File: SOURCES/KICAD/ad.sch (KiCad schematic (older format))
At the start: 154 parts, among them IC201 IC_OPA1652AIDR, IC202 IC_OPA1652AIDR, IC203 IC_OPA1652AIDR, IC204 IC_OPA1652AIDR, IC205 IC_AK5558VN, IC206 IC_OPA1652AIDR, IC207 IC_OPA1652AIDR, IC208 IC_OPA1652AIDR, IC209 IC_OPA1652AIDR, X201 CONN_02X13

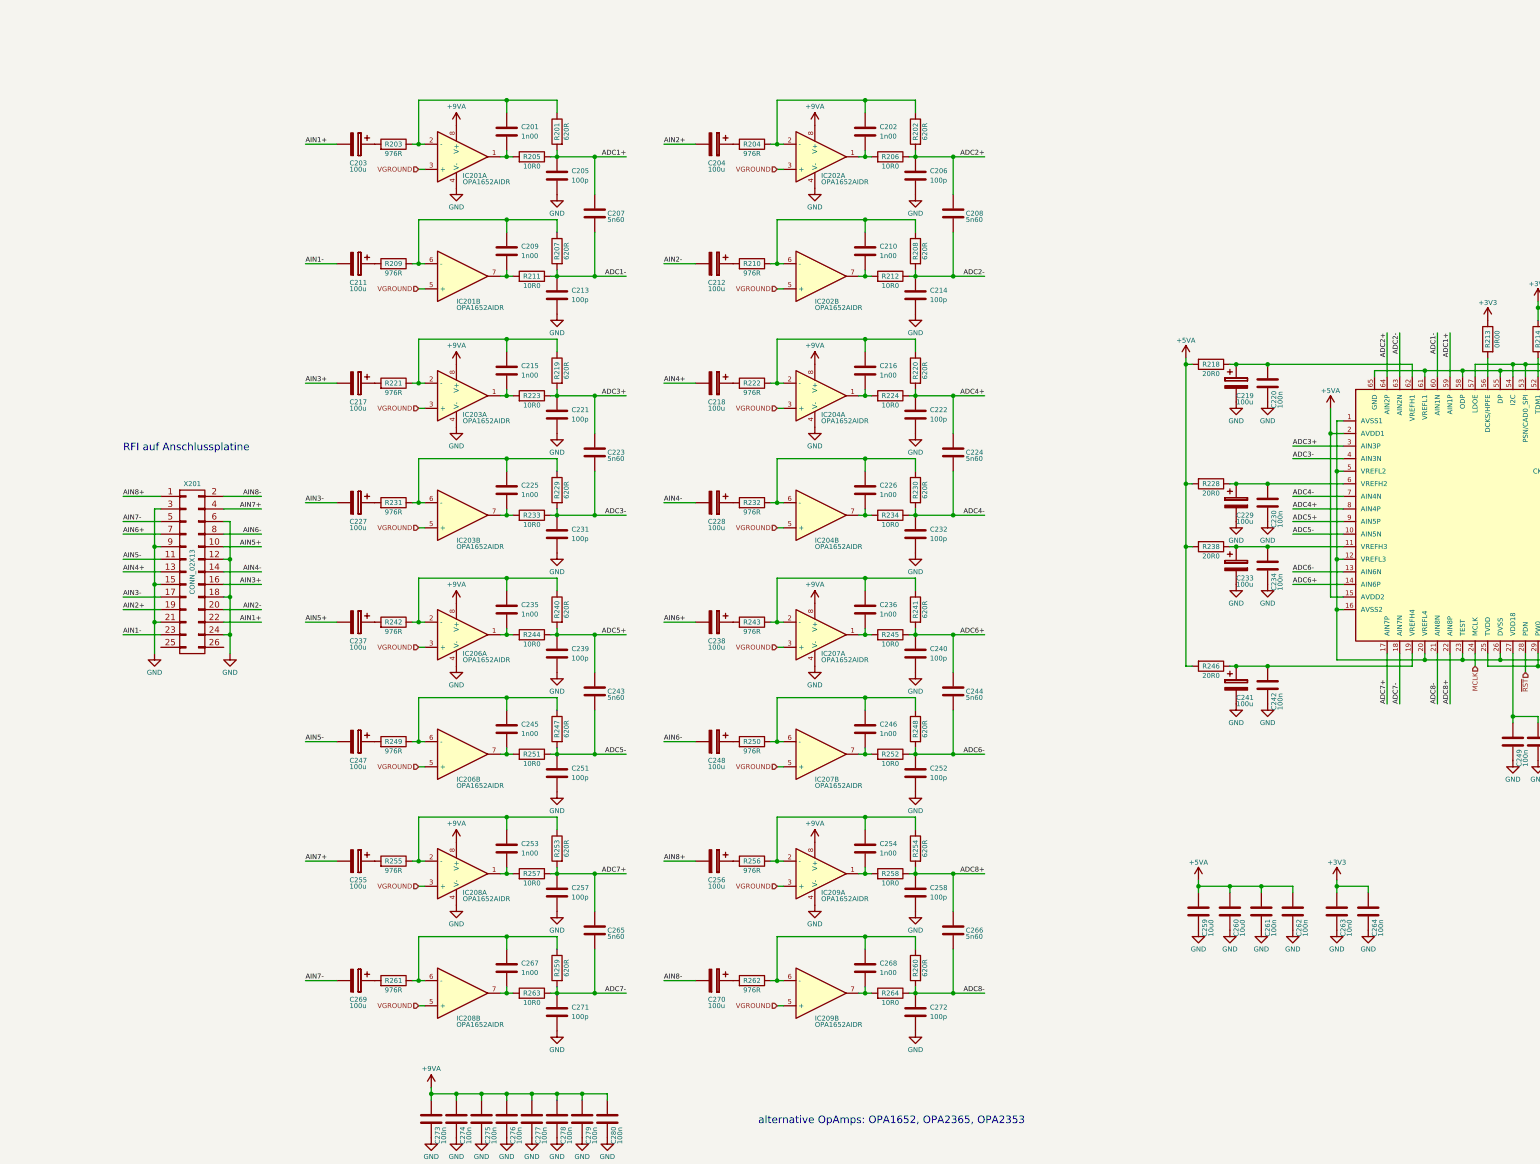
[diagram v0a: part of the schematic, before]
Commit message: Improved ADC input stage
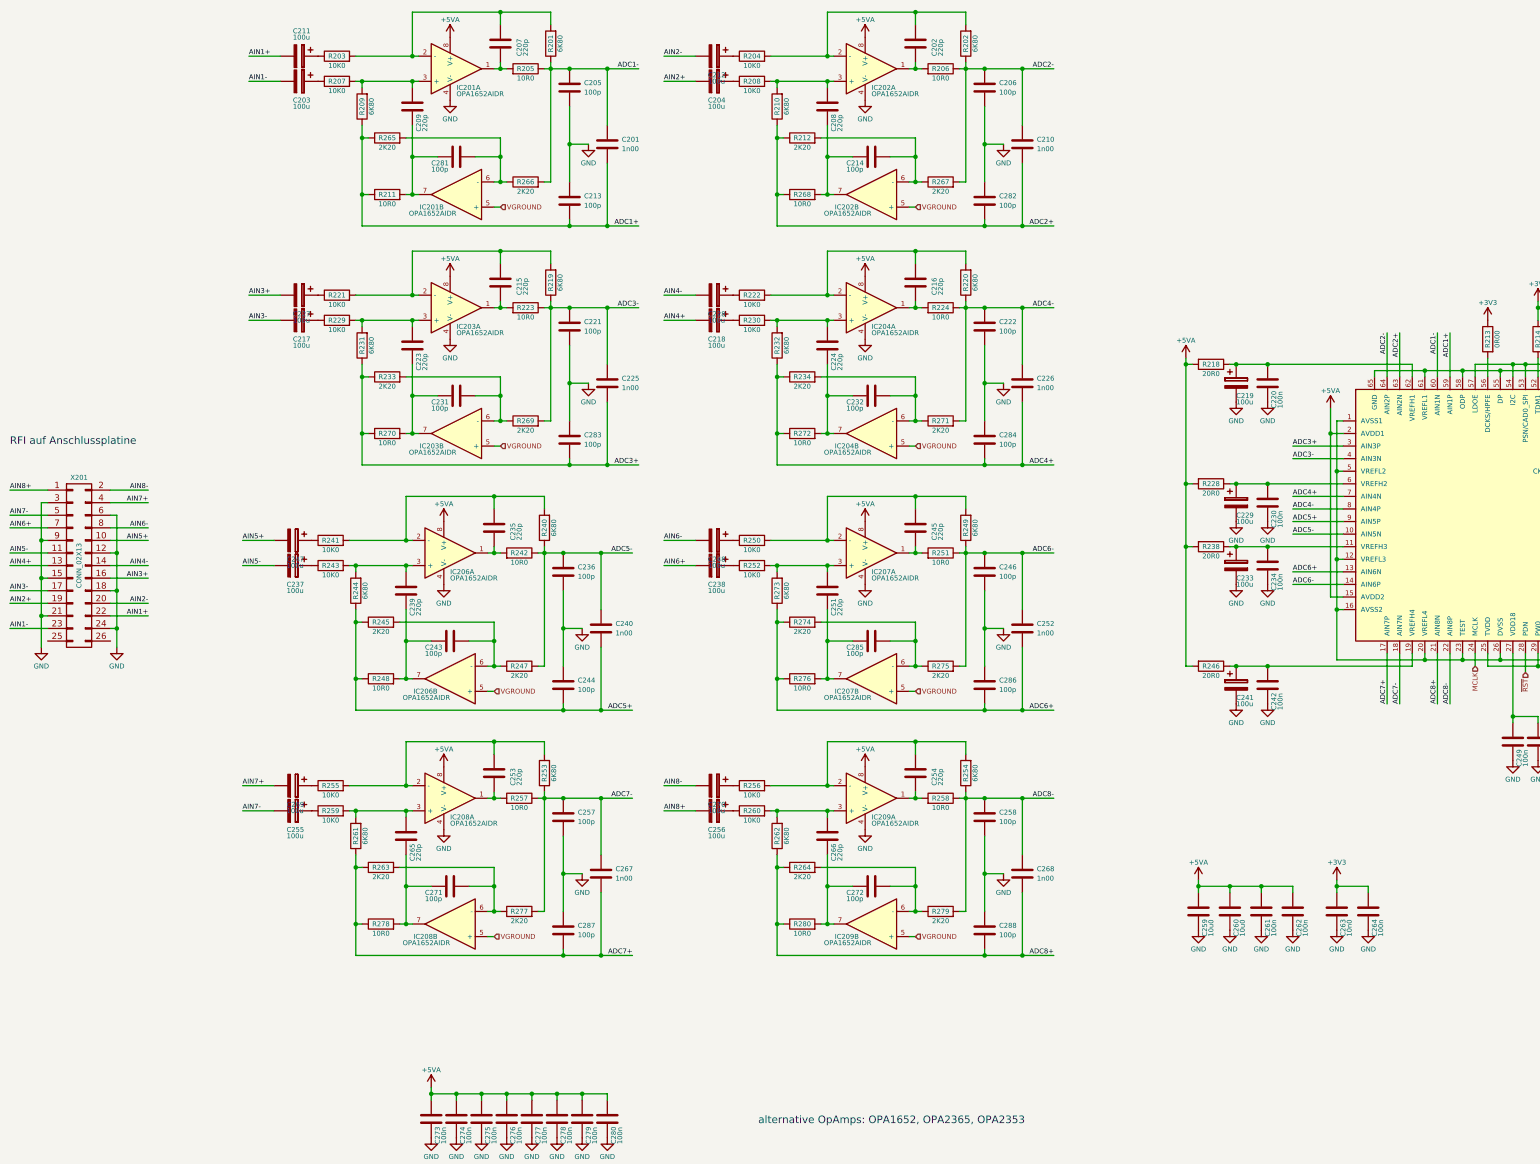
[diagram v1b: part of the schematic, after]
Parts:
- removed C207, C208, C223, C224, C243, C244, C265, C266: CAP_5n60_5%_16V_PPS_0805, rklib:C0805-X7R, symbol rk:CAP_5n60_5%_16V_PPS_0805
- removed C236, C246: CAP_1n00_5%_50V_PPS_0805, rklib:C0805-X7R, symbol rk:CAP_1n00_5%_50V_PPS_0805
- removed C239, C240, C251, C252: CAP_100p_50V_C0G_NP0_0805, rklib:C0805-X7R, symbol rk:CAP_100p_50V_C0G_NP0_0805
- removed R201, R202, R207, R208, R219, R220, R229, R230, R240, R241, R247, R248, R253, R254, R259, R260: RES_620R_0.5%_0.1W_Thin_0805, rklib:C0805-RES, symbol rk:RES_620R_0.5%_0.1W_Thin_0805
- removed R203, R204, R209, R210, R221, R222, R231, R232, R242, R243, R249, R250, R255, R256, R261, R262: RES_976R_0.5%_0.1W_Thin_0805, rklib:C0805-RES, symbol rk:RES_976R_0.5%_0.1W_Thin_0805
- removed R212, R233, R234, R244, R245, R252, R263, R264: RES_10R0_1%_0.25W_Thin_0805, rklib:C0805-RES, symbol rk:RES_10R0_1%_0.25W_Thin_0805
- added C207, C208, C223, C224, C239, C251, C265, C266: CAP_220p_2%_50V_PPS_0805, rklib:C0805-X7R, symbol rk:CAP_1n00_5%_50V_PPS_0805
- added C236, C243, C244, C246, C281, C282, C283, C284, C285, C286, C287, C288: CAP_100p_50V_C0G_NP0_0805, rklib:C0805-X7R, symbol rk:CAP_100p_50V_C0G_NP0_0805
- added C240, C252: CAP_1n00_5%_50V_PPS_0805, rklib:C0805-X7R, symbol rk:CAP_1n00_5%_50V_PPS_0805
- added R201, R202, R209, R210, R219, R220, R231, R232, R240, R244, R249, R253, R254, R261, R262, R273: RES_6K80_1%_0.25W_Thin_0805, rklib:C0805-RES, symbol rk:RES_10K0_1%_0.25W_Thin_0805
- added R203, R204, R207, R208, R221, R222, R229, R230, R241, R243, R250, R252, R255, R256, R259, R260: RES_10K0_1%_0.25W_Thin_0805, rklib:C0805-RES, symbol rk:RES_10K0_1%_0.25W_Thin_0805
- added R212, R233, R234, R245, R247, R263, R264, R265, R266, R267, R269, R271, R274, R275, R277, R279: RES_2K20_1%_0.25W_Thin_0805, rklib:C0805-RES, symbol rk:RES_10K0_1%_0.25W_Thin_0805
- added R242, R248, R268, R270, R272, R276, R278, R280: RES_10R0_1%_0.25W_Thin_0805, rklib:C0805-RES, symbol rk:RES_10R0_1%_0.25W_Thin_0805
- C202, C209, C215, C216, C235, C245, C253, C254: value CAP_1n00_5%_50V_PPS_0805 -> CAP_220p_2%_50V_PPS_0805; Value1 1n00 -> 220p; Value2 5% 50V PPS -> 2% 50V PPS; digikey PCF1328CT-ND -> PCF1288CT-ND; pn ECH-U1H102JX5 -> ECH-U1H221GX5
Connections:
- net +9VA is gone; now on net +5VA: C273.1, C274.1, C275.1, C276.1, C277.1, C278.1, C279.1, C280.1, IC201.8 (V+), IC202.8 (V+), IC203.8 (V+), IC204.8 (V+), IC206.8 (V+), IC207.8 (V+), IC208.8 (V+), IC209.8 (V+)
- net ADC1+: now also C201.2, C213.2, R211.1, R209.1, R265.1; no longer C205.1, R205.1
- net ADC1-: now also C201.1, C205.1, R205.1, R201.1, R266.2; no longer C213.1, R211.1
- net ADC2+: now also C210.2, IC205.63 (AIN2N), C282.2, R210.1, R212.1, R268.1; no longer C206.1, IC205.64 (AIN2P), R206.1
- net ADC2-: now also C206.1, C210.1, IC205.64 (AIN2P), R206.1, R202.1, R267.2; no longer C214.1, IC205.63 (AIN2N)
- net ADC3+: now also C225.2, C283.2, R231.1, R233.1, R270.1; no longer C221.1, R223.1
- net ADC3-: now also C221.1, C225.1, R223.1, R219.1, R269.2; no longer C231.1
- net ADC4+: now also C226.2, IC205.7 (AIN4N), C284.2, R232.1, R234.1, R272.1; no longer C222.1, IC205.8 (AIN4P), R224.1
- net ADC4-: now also C222.1, C226.1, IC205.8 (AIN4P), R224.1, R220.1, R271.2; no longer C232.1, IC205.7 (AIN4N)
- net ADC5+: now also C240.2, C244.2, R244.1, R245.1, R248.1
- net ADC5-: now also C236.1, C240.1, R240.1, R242.1, R247.2; no longer R251.1
- net ADC6+: now also IC205.13 (AIN6N), C252.2, C286.2, R273.1, R274.1, R276.1; no longer IC205.14 (AIN6P)
- net ADC6-: now also IC205.14 (AIN6P), R251.1, C246.1, C252.1, R249.1, R275.2; no longer IC205.13 (AIN6N)
- net ADC7+: now also C267.2, C287.2, R261.1, R263.1, R278.1; no longer C257.1, R257.1
- net ADC7-: now also C257.1, C267.1, R257.1, R253.1, R277.2; no longer C271.1
- net ADC8+: now also C268.2, IC205.21 (AIN8N), C288.2, R262.1, R264.1, R280.1; no longer C258.1, IC205.22 (AIN8P), R258.1
- net ADC8-: now also C258.1, C268.1, IC205.22 (AIN8P), R258.1, R254.1, R279.2; no longer C272.1, IC205.21 (AIN8N)
- net AIN1+: now also C211.2; no longer C203.2
- net AIN1-: now also C203.2; no longer C211.2
- net AIN3+: now also C227.2; no longer C217.2
- net AIN3-: now also C217.2; no longer C227.2
- net AIN5+: now also C247.2; no longer C237.2
- net AIN5-: now also C237.2; no longer C247.2
- net AIN7+: now also C269.2; no longer C255.2
- net AIN7-: now also C255.2; no longer C269.2
- net GND: now also C213.1, C236.2, C244.1, C246.2, C282.1, C283.1, C284.1, C286.1, C287.1, C288.1; no longer C213.2, C214.2, C231.2, C232.2, C271.2, C272.2
- net VGROUND: no longer IC201.3 (+), IC202.3 (+), IC203.3 (+), IC204.3 (+), IC206.3 (+), IC207.3 (+), IC208.3 (+), IC209.3 (+)
- net at C203.1: now also R207.1
- net at C204.1: now also R208.1
- net at C211.1: now also R203.1
- net at C212.1: now also R204.1
- net at C217.1: now also R229.1
- net at C227.1: now also R221.1
- net at C218.1: now also R230.1
- net at C228.1: now also R222.1
- net at C237.1: now also R243.1
- net at C247.1: now also R241.1
- net at C238.1: now also R252.1
- net at C248.1: now also R250.1
- net at C255.1: now also R259.1
- net at C256.1: now also R260.1
- net at C269.1: now also R255.1
- net at C270.1: now also R256.1
- net at IC201.1, R205.2: now also C207.2; no longer C201.2
- net at IC201.2 (-): now also C207.1, R201.2, R203.2; no longer C201.1
- net at C209.1: now also IC201.3 (+), R207.2, R209.2; no longer IC201.6 (-)
- net at C209.2, IC201.7, R211.2: now also C281.1
- net at C202.1, IC202.2 (-): now also R202.2, R204.2
- net at IC202.6 (-): now also C214.2, R212.2, R267.1; no longer C210.1
- net at IC202.7: now also C214.1, C208.2, R268.2; no longer C210.2
- net at C215.1, IC203.2 (-): now also R219.2, R221.2
- net at IC203.6 (-): now also C231.2, R233.2, R269.1; no longer C225.1
- net at IC203.7: now also C231.1, C223.2, R270.2; no longer C225.2
- net at C216.1, IC204.2 (-): now also R220.2, R222.2
- net at IC204.6 (-): now also C232.2, R234.2, R271.1; no longer C226.1
- net at IC204.7: now also C232.1, C224.2, R272.2; no longer C226.2
- net at C235.2, IC206.1: now also R242.2
- net at C235.1, IC206.2 (-): now also R240.2, R241.2
- net at IC206.6 (-): now also C243.2, R245.2, R247.1; no longer C245.1
- net at C245.2, R251.2: now also IC207.1; no longer IC206.7
- net at IC207.2 (-): now also C245.1, R249.2, R250.2
- net at IC207.6 (-): now also C285.2, R274.2, R275.1
- net at IC207.7: now also C251.2, C285.1, R276.2
- net at C253.1, IC208.2 (-): now also R253.2, R255.2
- net at IC208.6 (-): now also C271.2, R263.2, R277.1; no longer C267.1
- net at IC208.7: now also C271.1, C265.2, R278.2; no longer C267.2
- net at C254.1, IC209.2 (-): now also R254.2, R256.2
- net at IC209.6 (-): now also C272.2, R264.2, R279.1; no longer C268.1
- net at IC209.7: now also C272.1, C266.2, R280.2; no longer C268.2
- new net: C281.2, IC201.6 (-), R265.2, R266.1
- new net: C265.1, IC208.3 (+), R259.2, R261.2
- new net: C266.1, IC209.3 (+), R260.2, R262.2
- new net: C208.1, IC202.3 (+), R208.2, R210.2
- new net: C223.1, IC203.3 (+), R229.2, R231.2
- new net: C224.1, IC204.3 (+), R230.2, R232.2
- new net: C239.2, C243.1, IC206.7, R248.2
- new net: C239.1, IC206.3 (+), R243.2, R244.2
- new net: C251.1, IC207.3 (+), R252.2, R273.2
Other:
- moved on the sheet: C201, C203, C204, C205, C211, C212, C213, C217, C218, C227, C228, C237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
